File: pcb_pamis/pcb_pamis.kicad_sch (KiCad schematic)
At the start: 26 parts, among them J2 USB_A, J3 1755736, J7 Connecteur GPIO, Q1 Q_NPN_BEC, Q2 Q_NPN_BEC, SW1 SW_Push, U1 ESP32-WROOM-32UE, U2 CP2102N-Axx-xQFN28

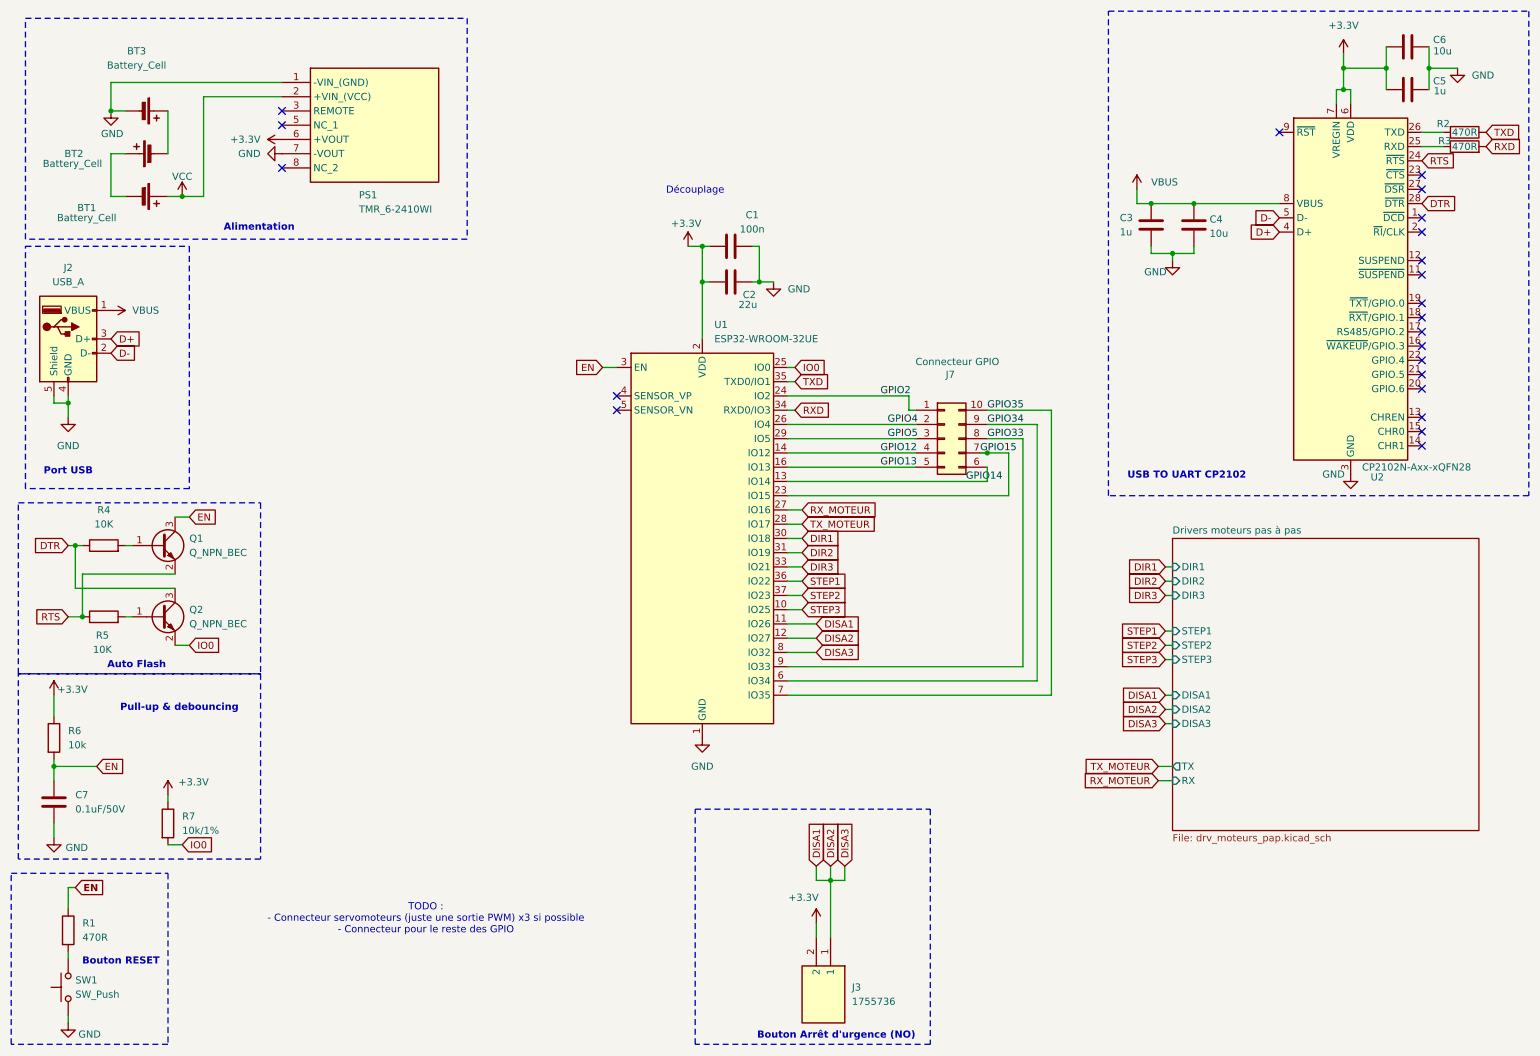
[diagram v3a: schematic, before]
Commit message: Ajout connecteurs, diodes sur arrêt moteurs et finalisation du schéma
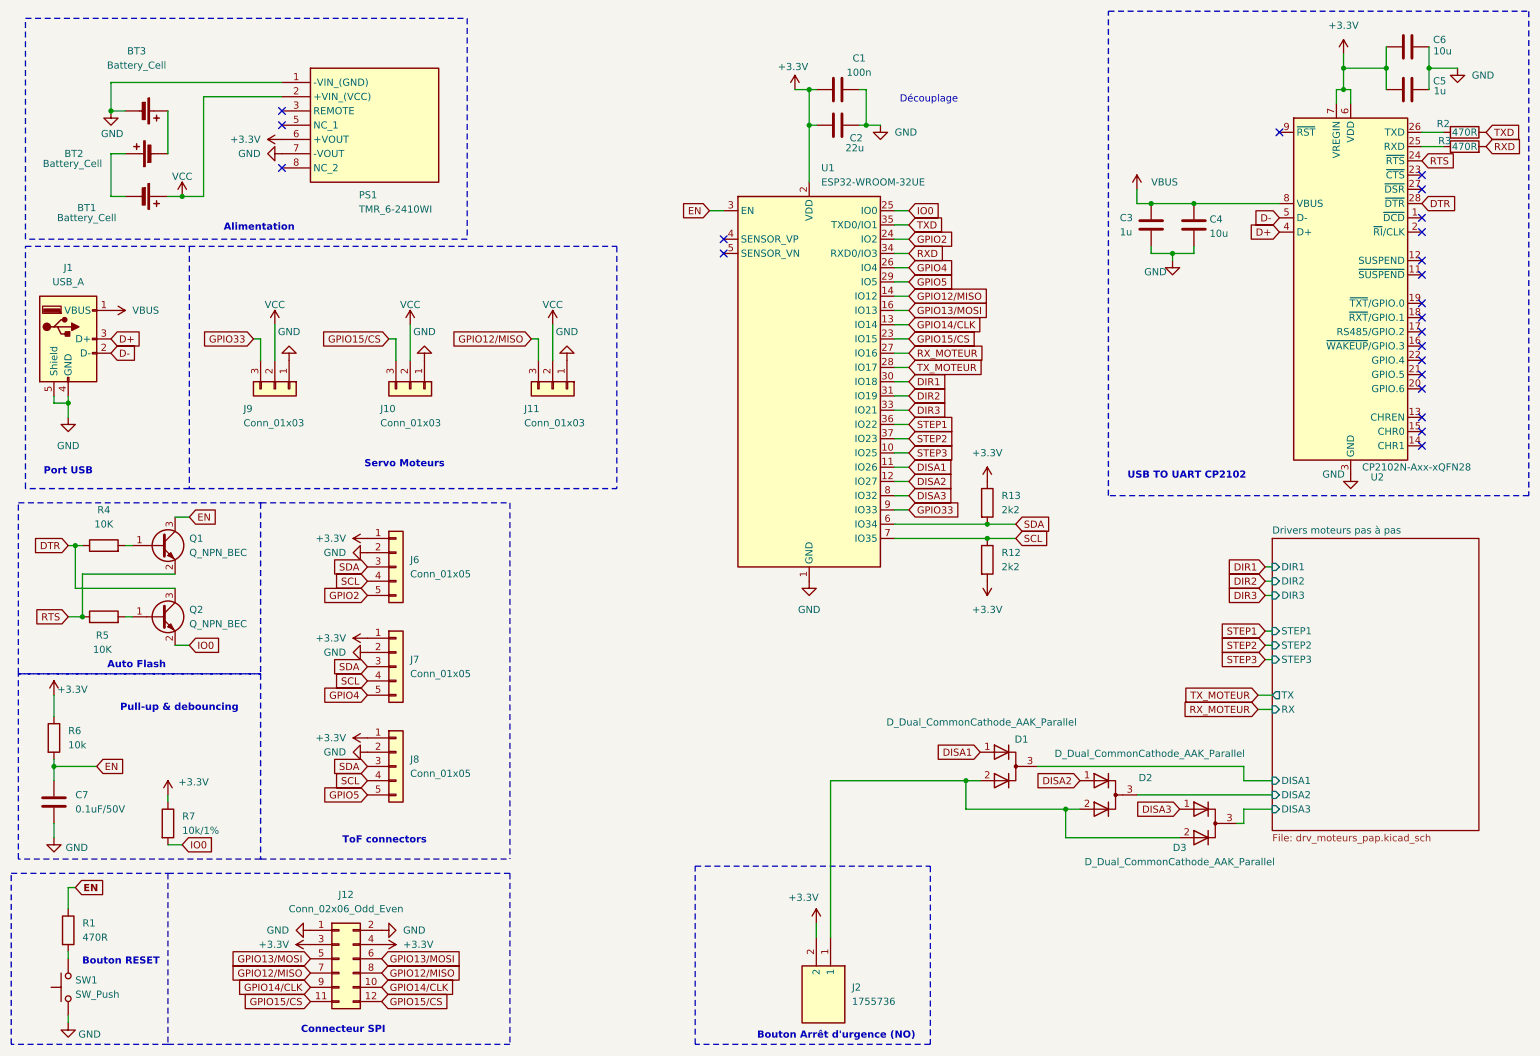
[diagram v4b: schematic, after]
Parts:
- removed J7: Connecteur GPIO, symbol Connector_Generic:Conn_02x05_Counter_Clockwise
- added D1, D2, D3: D_Dual_CommonCathode_AAK_Parallel, symbol Device:D_Dual_CommonCathode_AAK_Parallel
- added J10, J11, J9: Conn_01x03, symbol Connector_Generic:Conn_01x03
- added J12: Conn_02x06_Odd_Even, symbol Connector_Generic:Conn_02x06_Odd_Even
- added J6, J7, J8: Conn_01x05, symbol Connector_Generic:Conn_01x05
- added R12, R13: 2k2, symbol Device:R
- renumbered J2 to J1, J3 to J2
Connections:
- net +3.3V: now also J12.3 (Pin_3), J12.4 (Pin_4), J6.1 (Pin_1), J7.1 (Pin_1), J8.1 (Pin_1), R12.2, R13.1
- net DISA1: now also D1.1 (A); no longer J2.1, U1.12 (IO27), U1.8 (IO32)
- net GND: now also J10.1 (Pin_1), J11.1 (Pin_1), J12.1 (Pin_1), J12.2 (Pin_2), J6.2 (Pin_2), J7.2 (Pin_2), J8.2 (Pin_2), J9.1 (Pin_1)
- net GPIO2: now also J6.5 (Pin_5)
- net GPIO33: now also J9.3 (Pin_3)
- net GPIO4: now also J7.5 (Pin_5)
- net GPIO5: now also J8.5 (Pin_5)
- net VCC: now also J10.2 (Pin_2), J11.2 (Pin_2), J9.2 (Pin_2)
- net GPIO12 renamed GPIO12/MISO
- net GPIO12/MISO: now also J11.3 (Pin_3), J12.7 (Pin_7), J12.8 (Pin_8)
- net GPIO13 renamed GPIO13/MOSI
- net GPIO13/MOSI: now also J12.5 (Pin_5), J12.6 (Pin_6)
- net GPIO14 renamed GPIO14/CLK
- net GPIO14/CLK: now also J12.10 (Pin_10), J12.9 (Pin_9)
- net GPIO15 renamed GPIO15/CS
- net GPIO15/CS: now also J10.3 (Pin_3), J12.11 (Pin_11), J12.12 (Pin_12)
- net GPIO34 renamed SDA
- net SDA: now also J6.3 (Pin_3), J7.3 (Pin_3), J8.3 (Pin_3), R13.2
- net GPIO35 renamed SCL
- net SCL: now also J6.4 (Pin_4), J7.4 (Pin_4), J8.4 (Pin_4), R12.1
- new net: D1.2 (A), D2.2 (A), D3.2 (A), J2.1
- new net DISA2: D2.1 (A), U1.12 (IO27)
- new net DISA3: D3.1 (A), U1.8 (IO32)
- new net Drivers moteurs pas à pas/DISA1: D1.3 (K)
- new net Drivers moteurs pas à pas/DISA2: D2.3 (K)
- new net Drivers moteurs pas à pas/DISA3: D3.3 (K)
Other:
- note added: "Connecteur SPI"
- note added: "Servo Moteurs"
- note added: "ToF connectors"
- note removed: "TODO : - Connecteur servomoteurs (juste une sortie PWM) x3 si possible - Connecteur pour le reste des GPIO"
- moved on the sheet: C1, C2, U1

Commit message: ajout des empreintes pour le pcb PAMI
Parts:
- D1, D2, D3: footprint (none) -> Package_TO_SOT_SMD:TSOT-23_HandSoldering
- J10, J11, J9: footprint (none) -> Connector_PinHeader_1.27mm:PinHeader_1x03_P1.27mm_Vertical
- J12: footprint (none) -> Connector_PinHeader_1.27mm:PinHeader_2x06_P1.27mm_Vertical
- J6, J7, J8: footprint (none) -> Connector_PinHeader_1.27mm:PinHeader_1x05_P1.27mm_Vertical
- Q1, Q2: footprint (none) -> Package_TO_SOT_SMD:SOT-23_Handsoldering
- R1, R12, R13, R2, R3, R4, R5, R6, R7: footprint (none) -> Resistor_SMD:R_0805_2012Metric_Pad1.20x1.40mm_HandSolder
- SW1: footprint (none) -> Button_Switch_SMD:SW_Push_1P1T_NO_CK_KMR2
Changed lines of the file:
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@@
 			)
 		)
-		(property "Footprint" ""
+		(property "Footprint" "Connector_PinHeader_1.27mm:PinHeader_2x06_P1.27mm_Vertical"
 			(at 71.12 181.61 0)
 			(effects
@@
 			)
 		)
-		(property "Footprint" ""
+		(property "Footprint" "Resistor_SMD:R_0805_2012Metric_Pad1.20x1.40mm_HandSolder"
 			(at 271.78 32.512 90)
 			(effects
@@
 			)
 		)
-		(property "Footprint" ""
+		(property "Footprint" "Resistor_SMD:R_0805_2012Metric_Pad1.20x1.40mm_HandSolder"
 			(at 29.21 109.728 90)
 			(effects
@@
 			)
 		)
-		(property "Footprint" ""
+		(property "Footprint" "Button_Switch_SMD:SW_Push_1P1T_NO_CK_KMR2"
 			(at 17.78 186.69 0)
 			(effects
@@
 			)
 		)
-		(property "Footprint" ""
+		(property "Footprint" "Connector_PinHeader_1.27mm:PinHeader_1x03_P1.27mm_Vertical"
 			(at 83.82 80.01 0)
 			(effects
@@
 			)
 		)
-		(property "Footprint" ""
+		(property "Footprint" "Connector_PinHeader_1.27mm:PinHeader_1x05_P1.27mm_Vertical"
 			(at 81.28 111.76 0)
 			(effects
@@
 			)
 		)
-		(property "Footprint" ""
+		(property "Footprint" "Resistor_SMD:R_0805_2012Metric_Pad1.20x1.40mm_HandSolder"
 			(at 271.78 38.608 90)
 			(effects
@@
 			)
 		)
-		(property "Footprint" ""
+		(property "Footprint" "Connector_PinHeader_1.27mm:PinHeader_1x03_P1.27mm_Vertical"
 			(at 59.69 80.01 0)
 			(effects
@@
 			)
 		)
-		(property "Footprint" ""
+		(property "Footprint" "Package_TO_SOT_SMD:TSOT-23_HandSoldering"
 			(at 209.55 152.4 0)
 			(effects
@@
 			)
 		)
-		(property "Footprint" ""
+		(property "Footprint" "Resistor_SMD:R_0805_2012Metric_Pad1.20x1.40mm_HandSolder"
 			(at 184.912 110.49 90)
 			(effects
@@
 			)
 		)
-		(property "Footprint" ""
+		(property "Footprint" "Connector_PinHeader_1.27mm:PinHeader_1x03_P1.27mm_Vertical"
 			(at 109.22 80.01 0)
 			(effects
@@
 			)
 		)
-		(property "Footprint" ""
+		(property "Footprint" "Connector_PinHeader_1.27mm:PinHeader_1x05_P1.27mm_Vertical"
 			(at 81.28 147.32 0)
 			(effects
@@
 			)
 		)
-		(property "Footprint" ""
+		(property "Footprint" "Package_TO_SOT_SMD:SOT-23_Handsoldering"
 			(at 44.45 105.41 0)
 			(effects
@@
 			)
 		)
-		(property "Footprint" ""
+		(property "Footprint" "Resistor_SMD:R_0805_2012Metric_Pad1.20x1.40mm_HandSolder"
 			(at 29.21 122.428 90)
 			(effects
@@
 			)
 		)
-		(property "Footprint" ""
+		(property "Footprint" "Resistor_SMD:R_0805_2012Metric_Pad1.20x1.40mm_HandSolder"
 			(at 21.082 176.53 90)
 			(effects
@@
 			)
 		)
-		(property "Footprint" ""
+		(property "Footprint" "Package_TO_SOT_SMD:SOT-23_Handsoldering"
 			(at 44.45 118.11 0)
 			(effects
@@
 			)
 		)
-		(property "Footprint" ""
+		(property "Footprint" "Resistor_SMD:R_0805_2012Metric_Pad1.20x1.40mm_HandSolder"
 			(at 38.862 157.48 90)
 			(effects
@@
 			)
 		)
-		(property "Footprint" ""
+		(property "Footprint" "Package_TO_SOT_SMD:TSOT-23_HandSoldering"
 			(at 227.33 157.48 0)
 			(effects
@@
 			)
 		)
-		(property "Footprint" ""
+		(property "Footprint" "Package_TO_SOT_SMD:TSOT-23_HandSoldering"
 			(at 191.77 147.32 0)
 			(effects
@@
 			)
 		)
-		(property "Footprint" ""
+		(property "Footprint" "Resistor_SMD:R_0805_2012Metric_Pad1.20x1.40mm_HandSolder"
 			(at 18.542 142.24 90)
 			(effects
@@
 			)
 		)
-		(property "Footprint" ""
+		(property "Footprint" "Connector_PinHeader_1.27mm:PinHeader_1x05_P1.27mm_Vertical"
 			(at 81.28 129.54 0)
 			(effects
@@
 			)
 		)
-		(property "Footprint" ""
+		(property "Footprint" "Resistor_SMD:R_0805_2012Metric_Pad1.20x1.40mm_HandSolder"
 			(at 184.912 100.33 90)
 			(effects

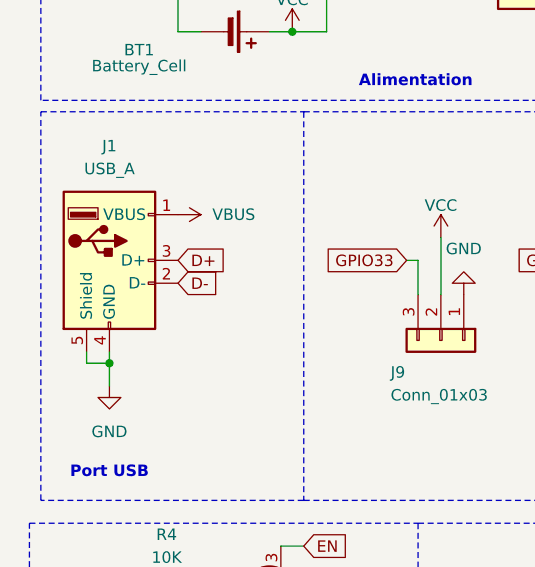
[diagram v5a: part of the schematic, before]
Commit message: finalisation empreintes des composants
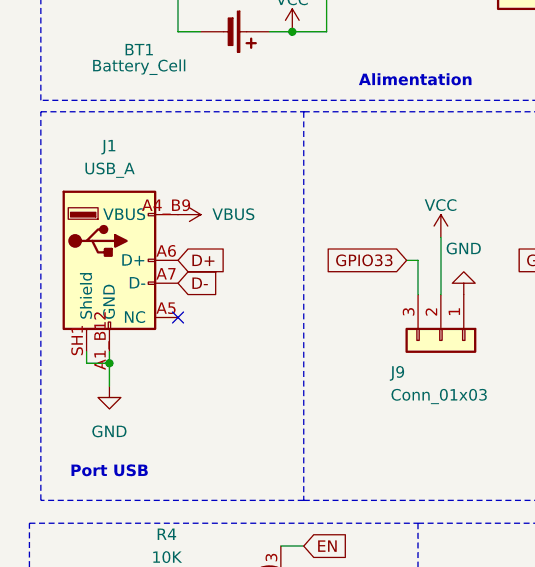
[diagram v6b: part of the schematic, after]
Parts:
- BT1, BT2, BT3: footprint (none) -> Modelec:BAT_1051_CR123A
- J1: footprint Connector_USB:USB_A_Receptacle_GCT_USB1046 -> Modelec:GCT_USB4105-GF-A
- J2: footprint 1755736 -> Modelec:PhoenixContact_MSTBVA_2,5_2-G-5,08_1x02_P5.08mm_Vertical
- SW1: footprint Button_Switch_SMD:SW_Push_1P1T_NO_CK_KMR2 -> Button_Switch_THT:SW_PUSH_6mm_H4.3mm
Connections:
- net D+: now also J1.A6 (D+), J1.B6 (D+); no longer J1.3 (D+)
- net D-: now also J1.A7 (D-), J1.B7 (D-); no longer J1.2 (D-)
- net GND: now also BT3.N (-), J1.A1_B12 (GND), J1.B1_A12 (GND), J1.SH1 (Shield), J1.SH2 (Shield), J1.SH3 (Shield), J1.SH4 (Shield); no longer BT3.2 (-), J1.4 (GND), J1.5 (Shield)
- net VBUS: now also J1.A4_B9 (VBUS), J1.B4_A9 (VBUS); no longer J1.1 (VBUS)
- net VCC: now also BT1.P (+); no longer BT1.1 (+)
- new net: BT2.N (-), BT3.P (+)
- new net: BT1.N (-), BT2.P (+)
- new net NC: J1.A5 (NC), J1.A8 (NC), J1.B5 (NC), J1.B8 (NC)
- no-connect marks 22 -> 23
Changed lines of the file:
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@@
 	)
 	(no_connect
+		(at 30.48 77.47)
+	)
+	(no_connect
 		(at 60.96 33.02)
 	)
@@
 			)
 		)
-		(property "Footprint" "1755736"
+		(property "Footprint" "Modelec:PhoenixContact_MSTBVA_2,5_2-G-5,08_1x02_P5.08mm_Vertical"
 			(at 63.83 194.31 0)
 			(effects
@@
 			)
 		)
-		(property "Footprint" "Button_Switch_SMD:SW_Push_1P1T_NO_CK_KMR2"
+		(property "Footprint" "Button_Switch_THT:SW_PUSH_6mm_H4.3mm"
 			(at 17.78 186.69 0)
 			(effects
@@
 	)
 	(symbol
+		(lib_name "Battery_Cell_1")
 		(lib_id "Device:Battery_Cell")
 		(at 35.56 30.48 270)
@@
 			)
 		)
-		(property "Footprint" ""
+		(property "Footprint" "Modelec:BAT_1051_CR123A"
 			(at 37.084 30.48 90)
 			(effects
@@
 			)
 		)
-		(pin "1"
+		(pin "N"
 		)
-		(pin "2"
+		(pin "P"
 		)
 		(instances
@@
 			)
 		)
-		(property "Footprint" "Connector_USB:USB_A_Receptacle_GCT_USB1046"
+		(property "Footprint" "Modelec:GCT_USB4105-GF-A"
 			(at 26.67 72.39 0)
 			(effects
@@
 		)
 		(property "Description" "USB Type A connector"
-			(at 22.86 71.12 0)
+			(at 22.86 72.644 0)
 			(effects
 				(font
@@
 			)
 		)
-		(pin "2"
+		(pin "B7"
 		)
-		(pin "4"
+		(pin "A1_B12"
 		)
-		(pin "5"
+		(pin "SH2"
 		)
-		(pin "1"
+		(pin "A4_B9"
 		)
-		(pin "3"
+		(pin "A7"
+		)
+		(pin "SH4"
+		)
+		(pin "SH1"
+		)
+		(pin "SH3"
+		)
+		(pin "B6"
+		)
+		(pin "A6"
+		)
+		(pin "B1_A12"
+		)
+		(pin "B4_A9"
+		)
+		(pin "A8"
+		)
+		(pin "A5"
+		)
+		(pin "B5"
+		)
+		(pin "B8"
 		)
 		(instances
@@
 	)
 	(symbol
+		(lib_name "Battery_Cell_2")
 		(lib_id "Device:Battery_Cell")
 		(at 38.1 38.1 90)
@@
 			)
 		)
-		(property "Footprint" ""
+		(property "Footprint" "Modelec:BAT_1051_CR123A"
 			(at 36.576 38.1 90)
 			(effects
@@
 			)
 		)
-		(pin "1"
+		(pin "P"
 		)
-		(pin "2"
+		(pin "N"
 		)
 		(instances
@@
 			)
 		)
-		(property "Footprint" ""
+		(property "Footprint" "Modelec:BAT_1051_CR123A"
 			(at 37.084 45.72 90)
 			(effects
@@
 			)
 		)
-		(pin "1"
+		(pin "N"
 		)
-		(pin "2"
+		(pin "P"
 		)
 		(instances

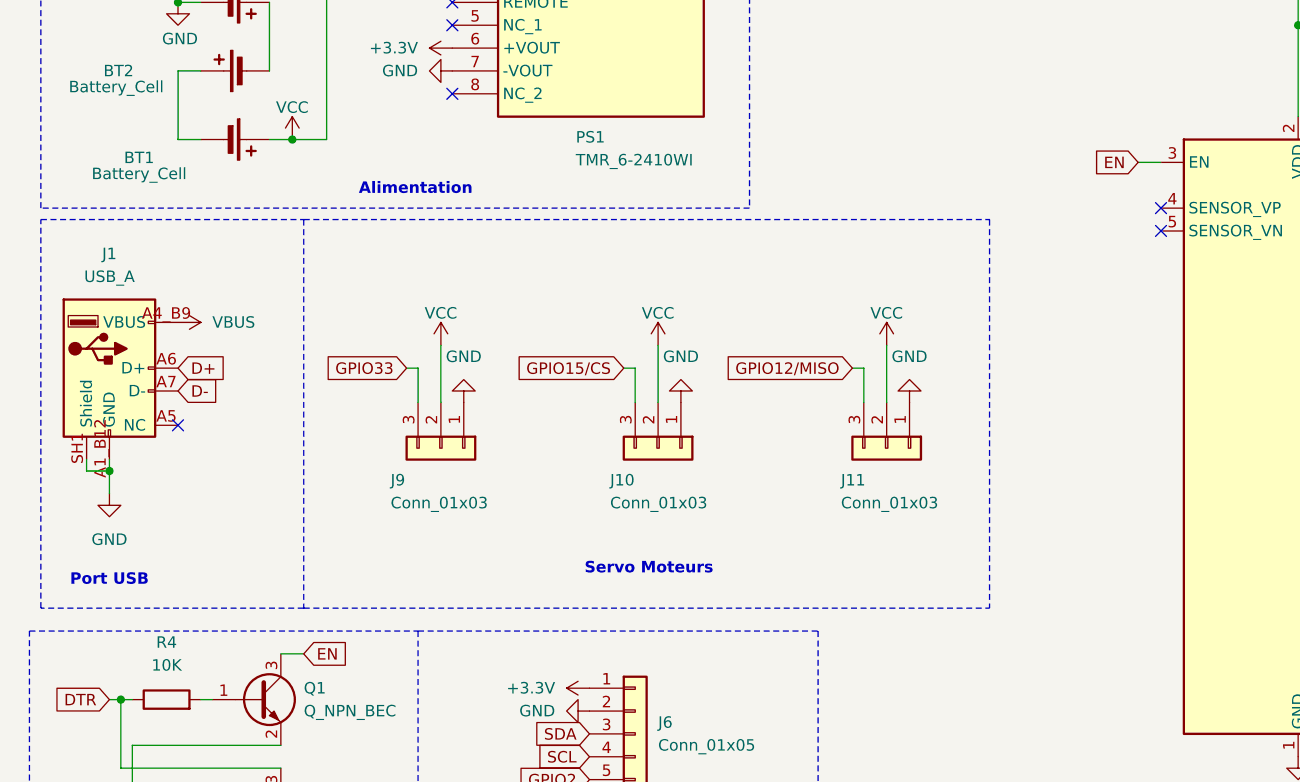
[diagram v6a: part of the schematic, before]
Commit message: remplacement usb A par type C sur schéma PAMI pour une meilleure cohérence avec le PCB
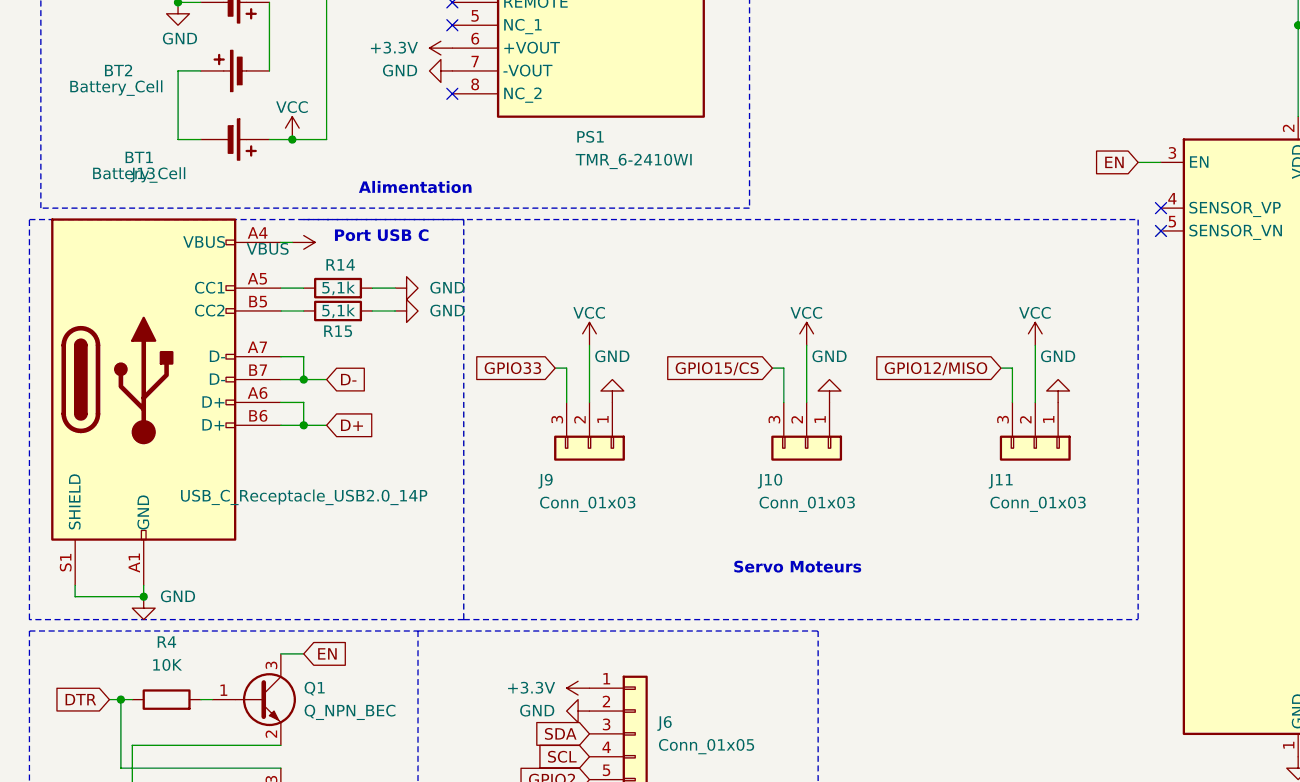
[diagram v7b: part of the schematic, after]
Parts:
- removed J1: USB_A, Modelec:GCT_USB4105-GF-A, symbol Connector:USB_A
- added J13: USB_C_Receptacle_USB2.0_14P, Modelec:GCT_USB4105-GF-A, symbol Connector:USB_C_Receptacle_USB2.0_14P
- added R14, R15: 5,1k, Resistor_SMD:R_0805_2012Metric_Pad1.20x1.40mm_HandSolder, symbol Device:R
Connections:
- net D+: now also J13.A6 (D+), J13.B6 (D+)
- net D-: now also J13.A7 (D-), J13.B7 (D-)
- net GND: now also J13.A1 (GND), J13.A12 (GND), J13.B1 (GND), J13.B12 (GND), J13.S1 (SHIELD), R14.2, R15.2
- net VBUS: now also J13.A4 (VBUS), J13.A9 (VBUS), J13.B4 (VBUS), J13.B9 (VBUS)
- new net: J13.B5 (CC2), R15.1
- new net: J13.A5 (CC1), R14.1
- no-connect marks 23 -> 22
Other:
- note added: "Port USB C"
- note removed: "Port USB"
- moved on the sheet: J10, J11, J9
